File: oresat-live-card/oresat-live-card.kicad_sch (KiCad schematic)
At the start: 7 parts

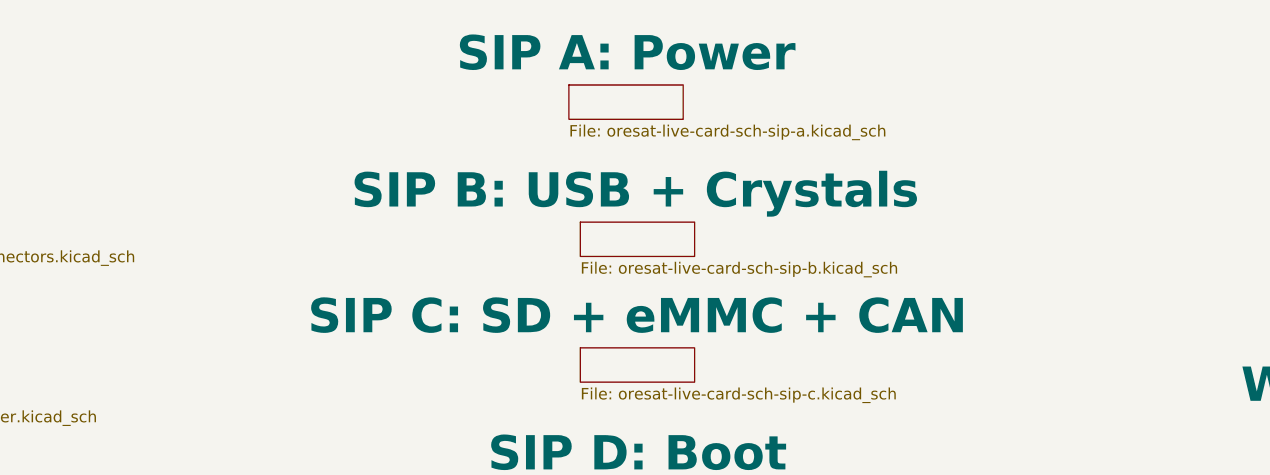
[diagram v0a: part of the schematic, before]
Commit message: Updated SIP A, B, and C. Lots of cleanup of crazy routing - this board is long in the tooth and has been rerouted several times, so there's a lot of crazy routing. Cleaning up a bit is really helping.
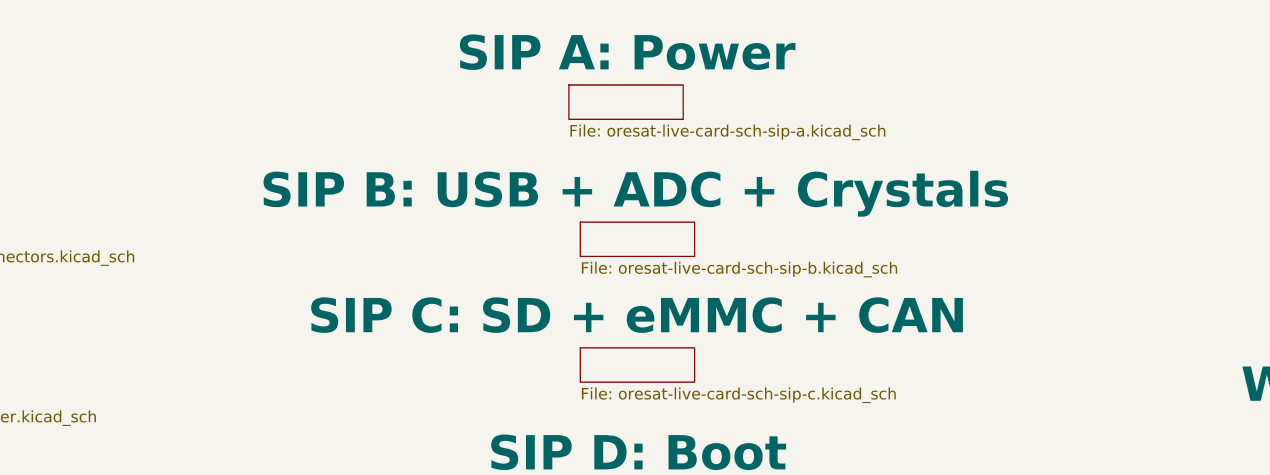
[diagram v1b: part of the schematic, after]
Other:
- sheet SIP B: USB + Crystals renamed SIP B: USB + ADC + Crystals
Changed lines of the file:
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@@
 			(color 0 0 0 0.0000)
 		)
-		(property "Sheetname" "SIP B: USB + Crystals"
+		(property "Sheetname" "SIP B: USB + ADC + Crystals"
 			(at 205.486 82.55 0)
 			(effects
